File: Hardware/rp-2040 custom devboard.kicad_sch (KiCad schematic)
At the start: 0 parts

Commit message: Wired the decoupling capacitors for the 2 power lines, the +3v3 and the +1v1 lines, now will work on the first major element, the power or the USB-C
git push
git push
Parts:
- added C1, C10: 1uF, symbol Device:C
- added C11, C12, C2, C3, C4, C5, C6, C7, C8, C9: 0.1uF, symbol Device:C
- added U1: RP2040, Package_DFN_QFN:QFN-56-1EP_7x7mm_P0.4mm_EP3.2x3.2mm, symbol MCU_RaspberryPi:RP2040
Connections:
- new net +1V1: C10.1, C11.1, C12.1, U1.23 (DVDD), U1.45 (VREG_VOUT), U1.50 (DVDD)
- new net +3V3: C1.1, C2.1, C3.1, C4.1, C5.1, C6.1, C7.1, C8.1, C9.1, U1.1 (IOVDD), U1.10 (IOVDD), U1.22 (IOVDD), U1.33 (IOVDD), U1.42 (IOVDD), U1.43 (ADC_AVDD), U1.44 (VREG_VIN), U1.48 (USB_VDD), U1.49 (IOVDD)
- new net GND: C1.2, C10.2, C11.2, C12.2, C2.2, C3.2, C4.2, C5.2, C6.2, C7.2, C8.2, C9.2, U1.57 (GND)

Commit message: Finished first working session, unfortunately interupted due to some external and uncontrollable circumstances (family visit lmao) but will continue later
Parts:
- added J1: USB_C_Receptacle_USB2.0_14P, symbol Connector:USB_C_Receptacle_USB2.0_14P
- added R1, R2: 5.1K, symbol Device:R
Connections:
- net GND: now also J1.A1 (GND), J1.A12 (GND), J1.B1 (GND), J1.B12 (GND), J1.S1 (SHIELD), R1.2, R2.2
- new net: J1.A4 (VBUS), J1.A9 (VBUS), J1.B4 (VBUS), J1.B9 (VBUS)
- new net: J1.A5 (CC1), R1.1
- new net: J1.B5 (CC2), R2.1
- new net USB_D+: J1.A6 (D+), J1.B6 (D+)
- new net USB_D-: J1.A7 (D-), J1.B7 (D-)

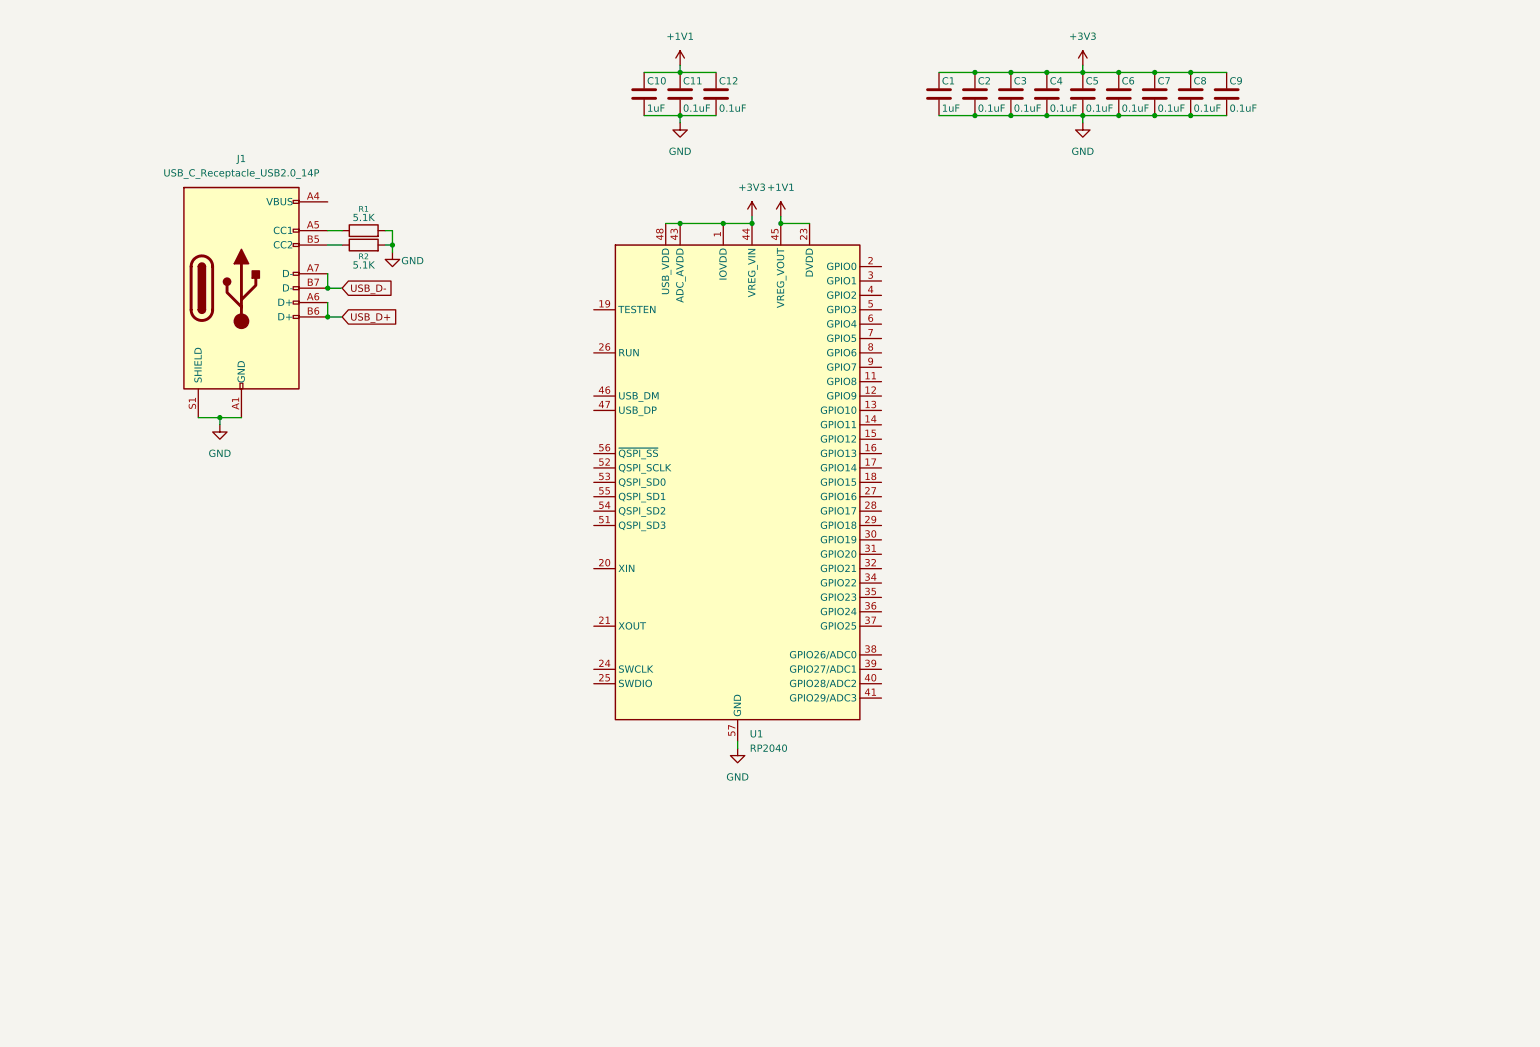
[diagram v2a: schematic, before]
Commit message: Placed LDO of the USB-C
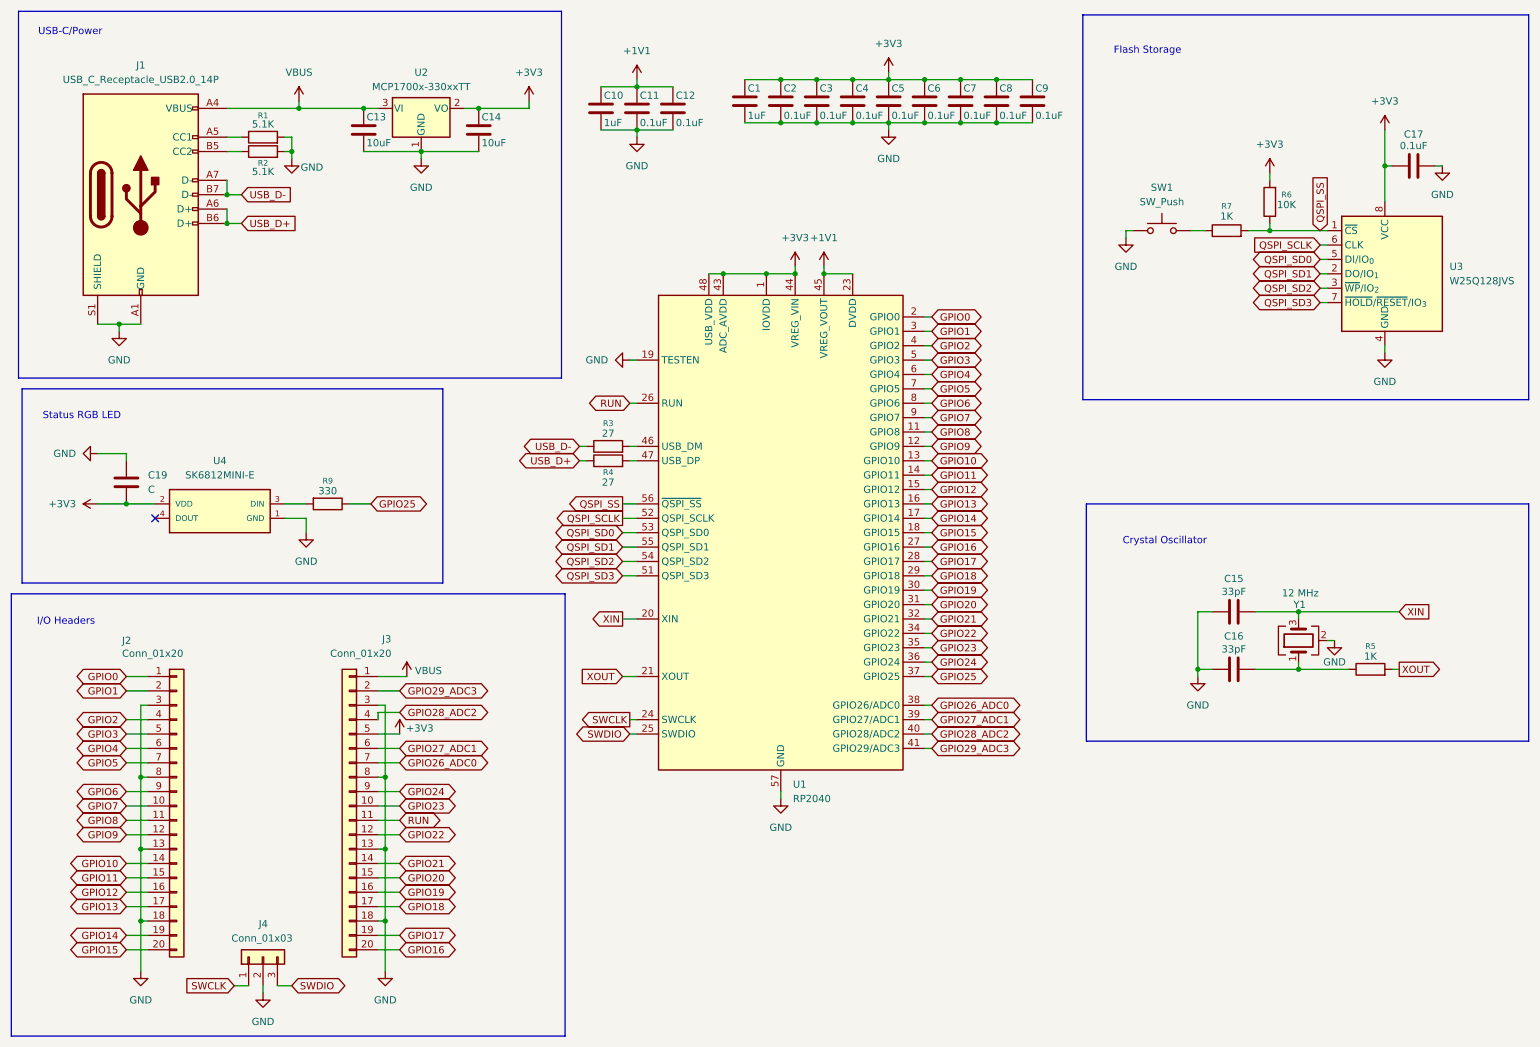
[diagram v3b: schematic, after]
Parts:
- added C13, C14: 10uF, symbol Device:C
- added C15, C16: 33pF, symbol Device:C
- added C17: 0.1uF, symbol Device:C
- added C19: C, symbol Device:C
- added J2, J3: Conn_01x20, symbol Connector_Generic:Conn_01x20
- added J4: Conn_01x03, symbol Connector_Generic:Conn_01x03
- added R3, R4: 27, symbol Device:R
- added R5, R7: 1K, symbol Device:R
- added R6: 10K, symbol Device:R
- added R9: 330, symbol Device:R
- added SW1: SW_Push, symbol Switch:SW_Push
- added U2: MCP1700x-330xxTT, Package_TO_SOT_SMD:SOT-23, symbol Regulator_Linear:MCP1700x-330xxTT
- added U3: W25Q128JVS, Package_SO:SOIC-8_5.3x5.3mm_P1.27mm, symbol Memory_Flash:W25Q128JVS
- added U4: SK6812MINI-E, symbol SK6812MINI-E:SK6812MINI-E
- added Y1: 12 MHz, symbol Device:Crystal_GND24
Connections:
- net +3V3: now also C14.1, C17.2, C19.2, J3.5 (Pin_5), R6.2, U2.2 (VO), U3.8 (VCC), U4.2 (VDD)
- net GND: now also U1.19 (TESTEN), C13.2, C14.2, C15.1, C16.1, C17.1, C19.1, J2.13 (Pin_13), J2.18 (Pin_18), J2.3 (Pin_3), J2.8 (Pin_8), J3.13 (Pin_13), J3.18 (Pin_18), J3.3 (Pin_3), J3.8 (Pin_8), J4.2 (Pin_2), SW1.1, U2.1 (GND), U3.4 (GND), U4.1 (GND), Y1.2 (G), Y1.4 (G)
- net USB_D+: now also R4.1
- net USB_D-: now also R3.1
- net VBUS: now reaches J1.A4 (VBUS), J1.A9 (VBUS), J1.B4 (VBUS), J1.B9 (VBUS)
- net VBUS: now also C13.1, J3.1 (Pin_1), U2.3 (VI)
- net GPIO8: now reaches U1.11 (GPIO8)
- net GPIO8: now also J2.11 (Pin_11)
- net GPIO9: now reaches U1.12 (GPIO9)
- net GPIO9: now also J2.12 (Pin_12)
- net GPIO10: now reaches U1.13 (GPIO10)
- net GPIO10: now also J2.14 (Pin_14)
- net GPIO11: now reaches U1.14 (GPIO11)
- net GPIO11: now also J2.15 (Pin_15)
- net GPIO12: now reaches U1.15 (GPIO12)
- net GPIO12: now also J2.16 (Pin_16)
- net GPIO13: now reaches U1.16 (GPIO13)
- net GPIO13: now also J2.17 (Pin_17)
- net GPIO14: now reaches U1.17 (GPIO14)
- net GPIO14: now also J2.19 (Pin_19)
- net GPIO15: now reaches U1.18 (GPIO15)
- net GPIO15: now also J2.20 (Pin_20)
- net GPIO0: now reaches U1.2 (GPIO0)
- net GPIO0: now also J2.1 (Pin_1)
- net XIN: now reaches U1.20 (XIN)
- net XIN: now also C15.2, Y1.3
- net XOUT: now reaches U1.21 (XOUT)
- net XOUT: now also R5.2
- net SWCLK: now reaches U1.24 (SWCLK)
- net SWCLK: now also J4.1 (Pin_1)
- net SWDIO: now reaches U1.25 (SWDIO)
- net SWDIO: now also J4.3 (Pin_3)
- net RUN: now reaches U1.26 (RUN)
- net RUN: now also J3.11 (Pin_11)
- net GPIO16: now reaches U1.27 (GPIO16)
- net GPIO16: now also J3.20 (Pin_20)
- net GPIO17: now reaches U1.28 (GPIO17)
- net GPIO17: now also J3.19 (Pin_19)
- net GPIO18: now reaches U1.29 (GPIO18)
- net GPIO18: now also J3.17 (Pin_17)
- net GPIO1: now reaches U1.3 (GPIO1)
- net GPIO1: now also J2.2 (Pin_2)
- net GPIO19: now reaches U1.30 (GPIO19)
- net GPIO19: now also J3.16 (Pin_16)
- net GPIO20: now reaches U1.31 (GPIO20)
- net GPIO20: now also J3.15 (Pin_15)
- net GPIO21: now reaches U1.32 (GPIO21)
- net GPIO21: now also J3.14 (Pin_14)
- net GPIO22: now reaches U1.34 (GPIO22)
- net GPIO22: now also J3.12 (Pin_12)
- net GPIO23: now reaches U1.35 (GPIO23)
- net GPIO23: now also J3.10 (Pin_10)
- net GPIO24: now reaches U1.36 (GPIO24)
- net GPIO24: now also J3.9 (Pin_9)
- net GPIO25: now reaches U1.37 (GPIO25)
- net GPIO25: now also R9.1
- net GPIO26_ADC0: now reaches U1.38 (GPIO26/ADC0)
- net GPIO26_ADC0: now also J3.7 (Pin_7)
- net GPIO27_ADC1: now reaches U1.39 (GPIO27/ADC1)
- net GPIO27_ADC1: now also J3.6 (Pin_6)
- net GPIO2: now reaches U1.4 (GPIO2)
- net GPIO2: now also J2.4 (Pin_4)
- net GPIO28_ADC2: now reaches U1.40 (GPIO28/ADC2)
- net GPIO28_ADC2: now also J3.4 (Pin_4)
- net GPIO29_ADC3: now reaches U1.41 (GPIO29/ADC3)
- net GPIO29_ADC3: now also J3.2 (Pin_2)
- net at U1.46 (USB_DM): now also R3.2
- net at U1.47 (USB_DP): now also R4.2
- net GPIO3: now reaches U1.5 (GPIO3)
- net GPIO3: now also J2.5 (Pin_5)
- net QSPI_SD3: now reaches U1.51 (QSPI_SD3)
- net QSPI_SD3: now also U3.7 (~{HOLD}/~{RESET}/IO_{3})
- net QSPI_SCLK: now reaches U1.52 (QSPI_SCLK)
- net QSPI_SCLK: now also U3.6 (CLK)
- net QSPI_SD0: now reaches U1.53 (QSPI_SD0)
- net QSPI_SD0: now also U3.5 (DI/IO_{0})
- net QSPI_SD2: now reaches U1.54 (QSPI_SD2)
- net QSPI_SD2: now also U3.3 (~{WP}/IO_{2})
- net QSPI_SD1: now reaches U1.55 (QSPI_SD1)
- net QSPI_SD1: now also U3.2 (DO/IO_{1})
- net QSPI_SS: now reaches U1.56 (~{QSPI_SS})
- net QSPI_SS: now also R6.1, R7.2, U3.1 (~{CS})
- net GPIO4: now reaches U1.6 (GPIO4)
- net GPIO4: now also J2.6 (Pin_6)
- net GPIO5: now reaches U1.7 (GPIO5)
- net GPIO5: now also J2.7 (Pin_7)
- net GPIO6: now reaches U1.8 (GPIO6)
- net GPIO6: now also J2.9 (Pin_9)
- net GPIO7: now reaches U1.9 (GPIO7)
- net GPIO7: now also J2.10 (Pin_10)
- new net: R9.2, U4.3 (DIN)
- new net: C16.2, R5.1, Y1.1
- new net: R7.1, SW1.2
- no-connect marks 0 -> 1
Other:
- note added: "Crystal Oscillator"
- note added: "Flash Storage"
- note added: "I/O Headers"
- note added: "Status RGB LED"
- note added: "USB-C/Power"
- moved on the sheet: C1, C10, C11, C12, C2, C3, C4, C5, C6, C7, C8, C9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

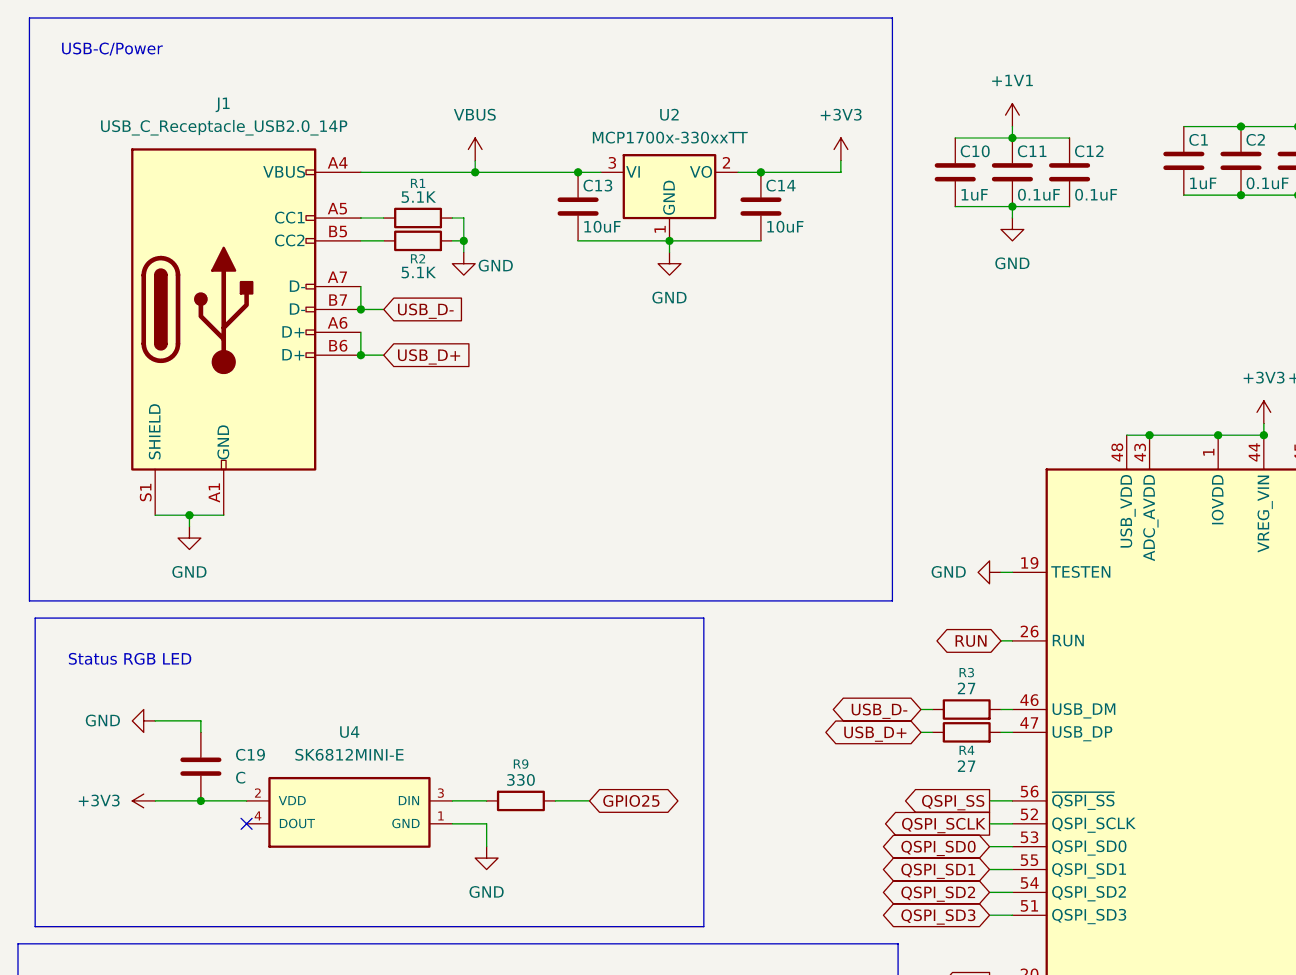
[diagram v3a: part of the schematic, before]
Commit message: There was a problem with the library of the SK6812MINI-E that i downloaded because the electrical type of the DIN pin was power input when it shouldve been just input, because its a data pin, anyways I fixed it so
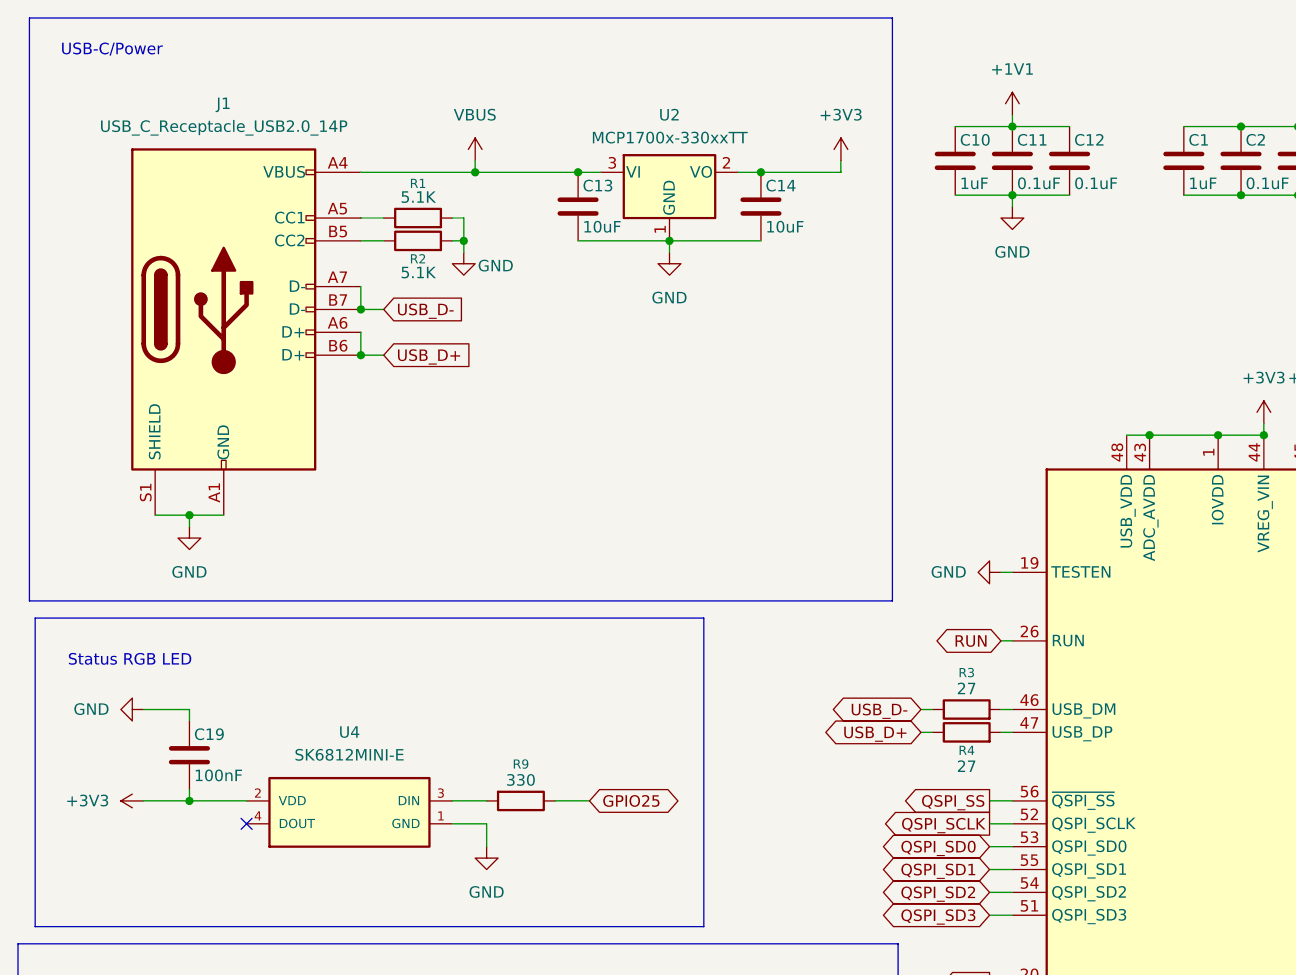
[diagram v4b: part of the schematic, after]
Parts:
- C19: value C -> 100nF
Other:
- moved on the sheet: C10, C11, C12, C19
